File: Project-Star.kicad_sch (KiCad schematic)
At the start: 215 parts, among them J1 J_TH1, J11 J_Flashing, J2 J_TH2, J3 Screw_Terminal_01x01, J4 Screw_Terminal_01x01, J5 Sense Terminals, J6 BMS_I2C, J7 Screw_Terminal_01x01, J8 Screw_Terminal_01x01, Q1 DMN2004K, Q10 ZXMP10A13F, Q13 ZXMP10A13F, Q14 CSD19531Q5A, Q15 CSD19531Q5A, Q16 CSD19531Q5A, Q17 CSD23381F4, Q18 TP0610K-T1-GE3, Q19 BSS138, Q2 DMN2004K, Q20 BSS123, Q3 DMN2004K, Q4 DMN2004K, Q5 CSD19531Q5A, Q6 DMN2004K, Q7 DMN2004K, Q8 DMN2004K, Q9 DMN2004K, SW1 Push_Button, SW2 Push_Button, SW3 SW_DPST, SW4 SW_DPST, U1 BQ7693006DBTR, U11 TPS3839G33DBZR, U2 BQ76200PW, U5 LMT01LPG, U6 MSP430G2553IPW28

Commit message: Restructured Layout
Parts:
- removed C1, C10, C11, C19, C2, C20, C21, C3, C31, C33, C34, C36, C37, C4, C5, C6, C74, C76, C8, C9: 100n, symbol Device:C
- removed C12, C40, C41: 10u, symbol Device:C
- removed C13, C18, C24, C38, C39, C7: 1u, symbol Device:C
- removed C14, C73: 4u7, symbol Device:C
- removed C15, C17: 4n7, symbol Device:C
- removed C16: 370p, symbol Device:C
- removed C22, C23: 10n, symbol Device:C
- removed C32: 2u2, symbol Device:C
- removed C75: 2.2n, symbol Device:C
- removed D1, D13, D18, D19, D20, D4, D61, D62, D63, D64, D7, D9: 5V6, symbol Device:D_Zener_Filled
- removed D10, D12, D14, D15, D29, D3, D31, D5, D6, D65, D66, D67, D68, D69, D70, D71, D8: LED, PCM_Diode_SMD_AKL:D_0805_2012Metric, symbol PCM_SL_Devices:LED
- removed D11, D17, D2, D27, D30: 3V3, symbol Device:D_Zener_Filled
- removed D16, D25, D26, D28, D35: 1N4148W, PCM_Diode_SMD_AKL:D_SOD-123, symbol PCM_Diode_AKL:1N4148W
- removed D24: 18V, symbol Device:D_Zener_Filled
- removed D59, D60: PTVS40VS1UTR, PCM_Diode_SMD_AKL:D_SOD-123F, symbol PCM_Diode_TVS_AKL:PTVS40VS1UTR
- removed E1: SparkGap, symbol Device:SparkGap
- removed FB1, FB2, FB3, FB4: 600R, symbol Device:FerriteBead_Small
- removed J1: J_TH1, 4ms_Connector:Pins_1x02_2.54mm_TH, symbol PCM_4ms_Connector:Conn_01x02
- removed J11: J_Flashing, 4ms_Connector:Pins_2x04_2.54mm_TH, symbol PCM_4ms_Connector:Conn_02x04
- removed J2: J_TH2, 4ms_Connector:Pins_1x02_2.54mm_TH, symbol PCM_4ms_Connector:Conn_01x02
- removed J3, J4, J7, J8: Screw_Terminal_01x01, symbol Connector:Screw_Terminal_01x01
- removed J5: Sense Terminals, 4ms_Connector:Pins_1x09_2.54mm_TH, symbol PCM_4ms_Connector:Conn_01x09
- removed J6: BMS_I2C, symbol Connector_Generic:Conn_01x05
- removed NT1: NetTie_2, symbol Device:NetTie_2
- removed Q1, Q2, Q3, Q4, Q6, Q7, Q8, Q9: DMN2004K, PCM_Package_TO_SOT_SMD_AKL:SOT-23, symbol PCM_Transistor_MOSFET_AKL:DMN2004K
- removed Q10, Q13: ZXMP10A13F, PCM_Package_TO_SOT_SMD_AKL:SOT-23, symbol PCM_Transistor_MOSFET_AKL:ZXMP10A13F
- removed Q14, Q15, Q16, Q5: CSD19531Q5A, Package_TO_SOT_SMD:TDSON-8-1, symbol Transistor_FET:CSD19531Q5A
- removed Q17: CSD23381F4, symbol Device:Q_PMOS
- removed Q18: TP0610K-T1-GE3, PCM_Package_TO_SOT_SMD_AKL:SOT-23, symbol PCM_Transistor_MOSFET_AKL:TP0610K
- removed Q19: BSS138, PCM_Package_TO_SOT_SMD_AKL:SOT-23, symbol PCM_Transistor_MOSFET_AKL:BSS138
- removed Q20: BSS123, PCM_Package_TO_SOT_SMD_AKL:SOT-23, symbol PCM_Transistor_MOSFET_AKL:BSS123
- removed R1, R11, R15, R24, R38, R40, R42, R5, R62, R83, R87: 10k, symbol Device:R
- removed R10, R12, R14, R16, R18, R19, R2, R21, R22, R23, R25, R27, R29, R31, R32, R37, R39, R4, R41, R44, R45, R46, R51, R6, R65, R7, R85, R86, R93, R98: 1k, symbol Device:R
- removed R100, R36, R43, R47, R48, R73, R74, R75, R76, R77, R78, R79, R80, R97, R99: 100R, symbol Device:R
- removed R13, R17, R26, R28, R3, R30, R8, R9: 33R, symbol Device:R
- removed R20: 510k, symbol Device:R
- removed R33, R34: 4k7, symbol Device:R
- removed R49, R50: 4R7, symbol Device:R
- removed R59, R70: 1M, symbol Device:R
- removed R60: 10M, symbol Device:R
- removed R61: 360k, symbol Device:R
- removed R63: 100, symbol Device:R
- removed R64: 3k01, symbol Device:R
- removed R66, R67, R68, R94: 2m, symbol Device:R
- removed R69, R71, R72, R88, R89, R90, R91, R92, R96: 100k, symbol Device:R
- removed R82: 47k, symbol Device:R
- removed R84: 154k, symbol Device:R
- removed R95: 0R, symbol Device:R
- removed SW1, SW2: Push_Button, Button_Switch_THT:SW_PUSH_6mm, symbol PCM_SL_Devices:Push_Button
- removed SW3, SW4: SW_DPST, symbol Switch:SW_DPST
- removed TH1, TH2: 10k NTC, symbol Device:Thermistor
- removed U1: BQ7693006DBTR, Package_SO:TSSOP-30_4.4x7.8mm_P0.5mm, symbol Battery_Management:BQ76930DBT
- removed U11: TPS3839G33DBZR, Package_TO_SOT_SMD:SOT-23, symbol Power_Supervisor:TPS3839DBZ
- removed U2: BQ76200PW, Package_SO:TSSOP-16_4.4x5mm_P0.65mm, symbol Battery_Management:BQ76200PW
- removed U5: LMT01LPG, Package_TO_SOT_THT:TO-92-2, symbol Sensor_Temperature:LMT01LPG
- removed U6: MSP430G2553IPW28, Package_SO:TSSOP-28_4.4x9.7mm_P0.65mm, symbol MCU_Texas_MSP430:MSP430G2553IPW28
- added J12, J13: Screw_Terminal_01x01, symbol Connector:Screw_Terminal_01x01
- added J9: Sense Terminals, 4ms_Connector:Pins_1x09_2.54mm_TH, symbol PCM_4ms_Connector:Conn_01x09
- added SW5: SW_DPST, symbol Switch:SW_DPST
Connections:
- net C0: now also J9.1 (Pin_1)
- net C1: now also J9.2 (Pin_2)
- net C2: now also J9.3 (Pin_3)
- net C3: now also J9.4 (Pin_4)
- net C4: now also J9.5 (Pin_5)
- net C5: now also J9.6 (Pin_6)
- net C6: now also J9.7 (Pin_7)
- net C7: now also J9.8 (Pin_8)
- net C8: now also J9.9 (Pin_9)
- net SCREW_BATT+: now also SW5.4
- new net: J13.1 (Pin_1), SW5.1
- new net: J12.1 (Pin_1), SW5.3
- new net SCREW_BATT-: SW5.2
- no-connect marks 1 -> 0
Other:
- added sheet BMS Protection Board (BMS Protection Board.kicad_sch)
- sheet USB-C-PD3.0 ports: added none; removed I2Ct_SCL, I2Ct_SDA
- note removed: "BMS Protection Board for 8S Battery Pack In/Out: min voltage: 24.0 V, nominal voltage: 29.6 V, max voltage: 33.6 V Output: 30A continuous discharge current, 100A peak discharge current"
- note removed: "Balancing & BMC"
- note removed: "Battery Level LEDs"
- note removed: "Battery Management System Controller"
- note removed: "CONN Headers"
- note removed: "Current Sense Filtering"
- note removed: "From TIDA-00449"
- note removed: "From TIDA-00449 / TIDA-010030"
- note removed: "From slua749a"
- note removed: "From slua810"
- note removed: "From slusc16b"
- note removed: "From slva729a"
- note removed: "From slva729a VDDCP was picked"
- note removed: "High Voltage REGSRC Supply"
- note removed: "High-Side Gate Driver"
- note removed: "I2C Pullups"
- note removed: "Interrupt for new current readings or errors"
- note removed: "JTAG/SBW"
- note removed: "MCU Current Sense"
- note removed: "PD I2C Lines have pullup's already"
- note removed: "PWR FLAGs"
- note removed: "Pack Switching and Current Sensing"
- note removed: "Passive Balancing Circuit"
- note removed: "REGOUT supplys 3v3"
- note removed: "Read Voltage"
- note removed: "Screw Terminals"
- note removed: "TODO: Add USB-C to Flash board"
- note removed: "Temperature Sensor"
- note removed: "Thermistors"
- note removed: "Understand how this works"
- note removed: "VC0-VSS (Vin max 3V6)"
- note removed: "Voltage Supervisor"
- note removed: "Wake-Up"
- note removed: "from TIDA-010030"
- note removed: "from slua810"
- note removed: "system is on LED"

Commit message: worked on MCU
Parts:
- added J3, J4: Screw_Terminal_01x01, symbol Connector:Screw_Terminal_01x01
- added SW2: SW_DPST, symbol Switch:SW_DPST
- renumbered J12 to J1, J13 to J2, J9 to J5, SW5 to SW1
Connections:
- net PACK+: now also SW2.4
- net PACK-: now also SW2.2
- net SCREW_BATT+ renamed BATT+
- net SCREW_BATT- renamed BATT-
- new net: J4.1 (Pin_1), SW2.1
- new net: J3.1 (Pin_1), SW2.3
- no-connect marks 0 -> 2
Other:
- removed sheet USB-C-PD3.0
- added sheet Power Management System Controller (Power Management System Controller.kicad_sch)
- added sheet USB-C PD 3.0 Source (USB-C PD 3.0 Source.kicad_sch)
- added sheet USB-C PD 3.1 Sink (USB-C PD 3.1 Sink.kicad_sch)
- sheet BMS Protection Board ports: added ALERT, BATT+, BATT-, CHG_EN, CP_EN, DSG_EN, ISENSE, PACK_READ_STATS, PACK_V, PCHG_EN, READ_ISENSE, REGOUT, SCL, SDA, TEMP, WAKE; removed SCREW_BATT+, SCREW_BATT-
- moved on the sheet: J1, J2, J5, SW1

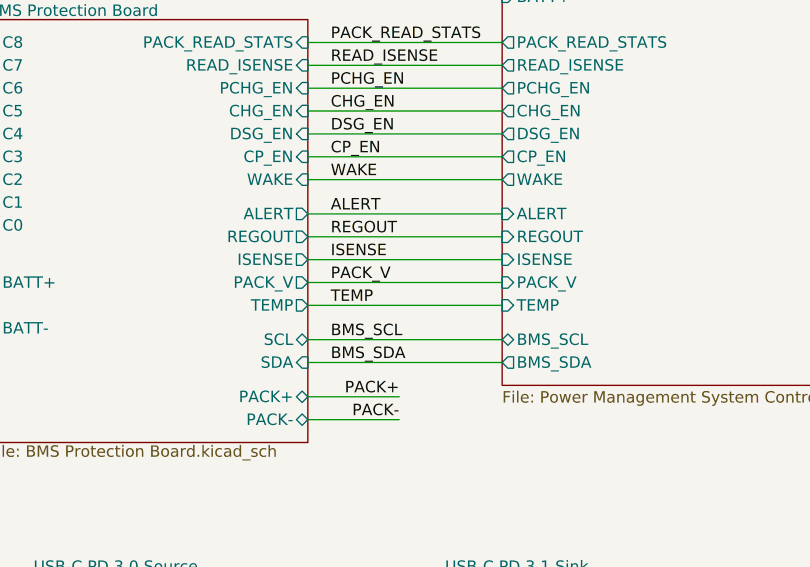
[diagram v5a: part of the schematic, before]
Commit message: commit before simplifying and removing features
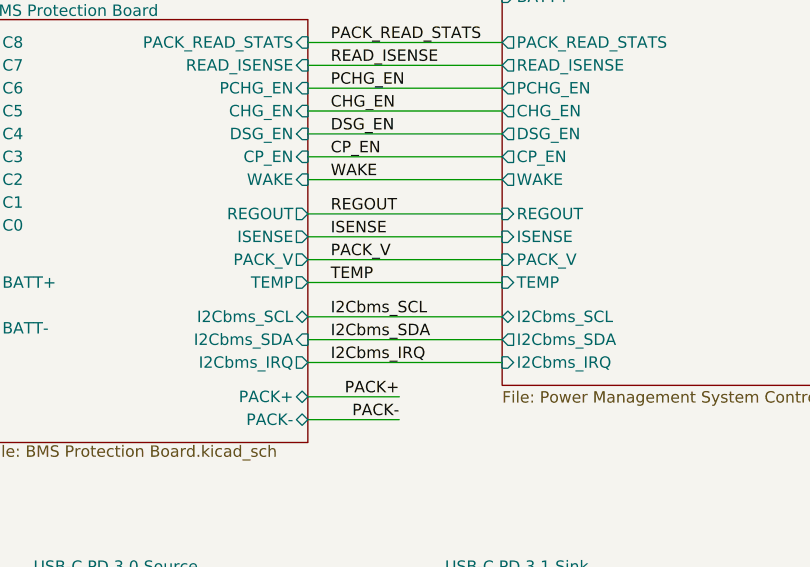
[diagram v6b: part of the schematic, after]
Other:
- sheet BMS Protection Board ports: added I2Cbms_IRQ, I2Cbms_SCL, I2Cbms_SDA; removed ALERT, SCL, SDA
- sheet Power Management System Controller ports: added I2Cbms_IRQ, I2Cbms_SCL, I2Cbms_SDA; removed ALERT, BMS_SCL, BMS_SDA

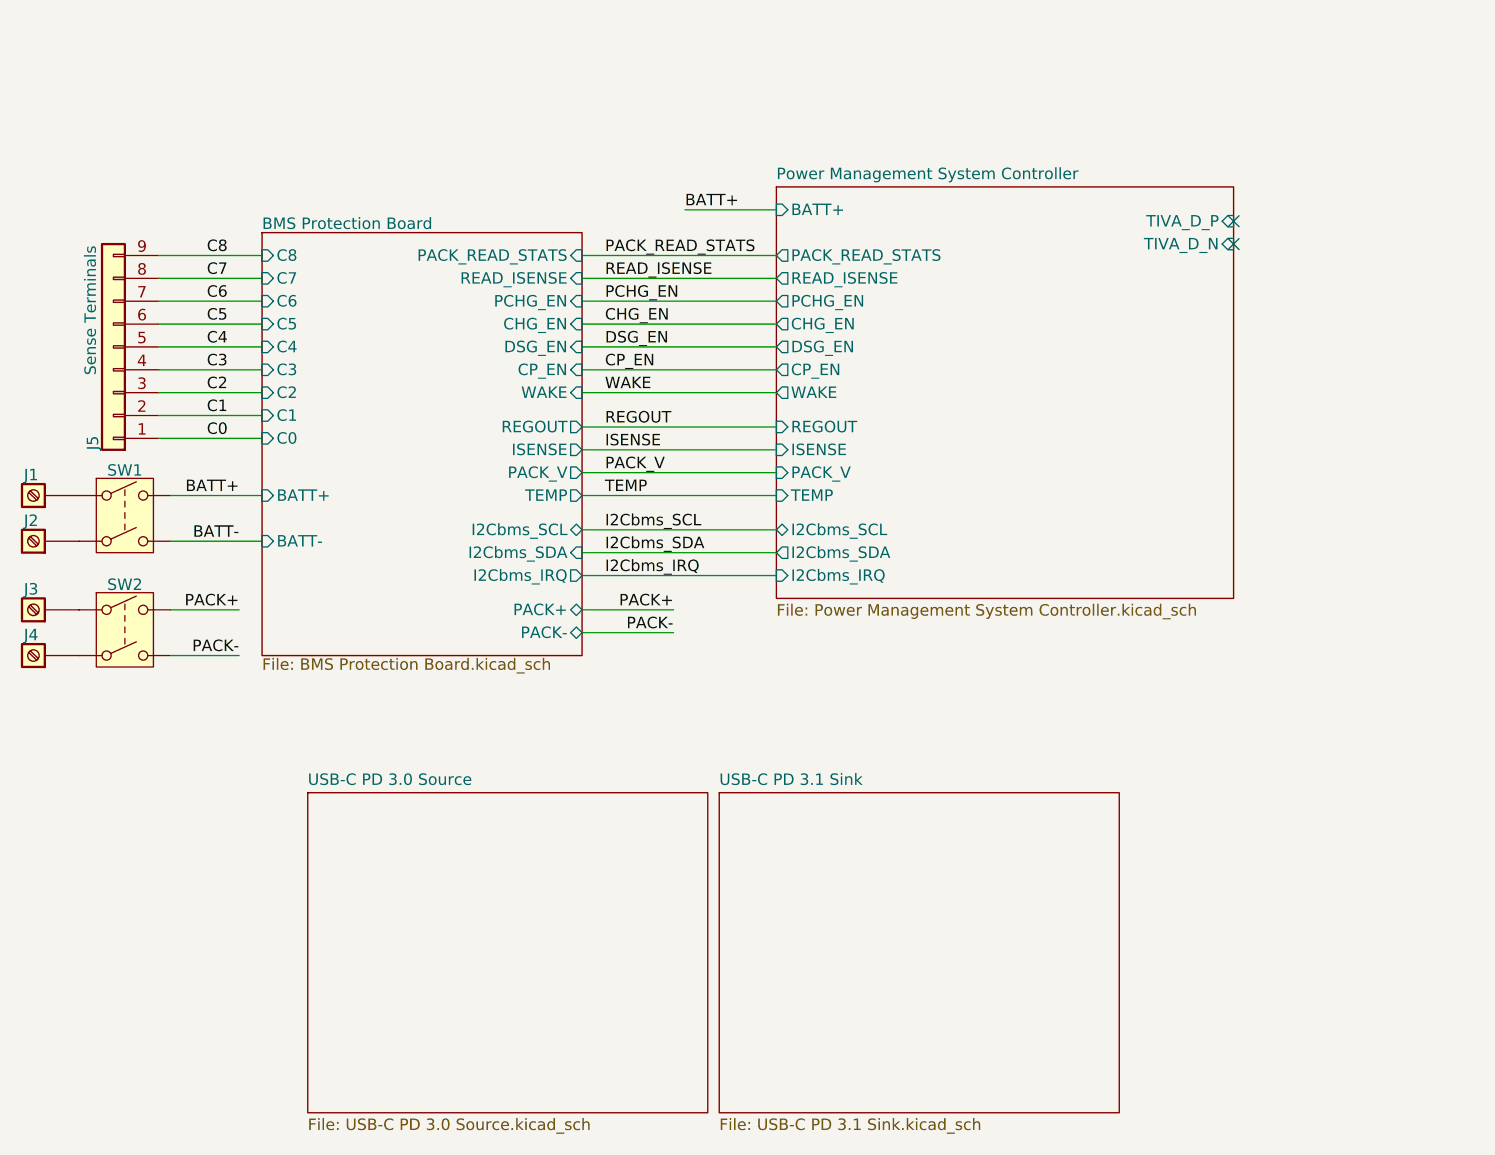
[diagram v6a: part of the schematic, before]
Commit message: Added Fuel/Gas Guage
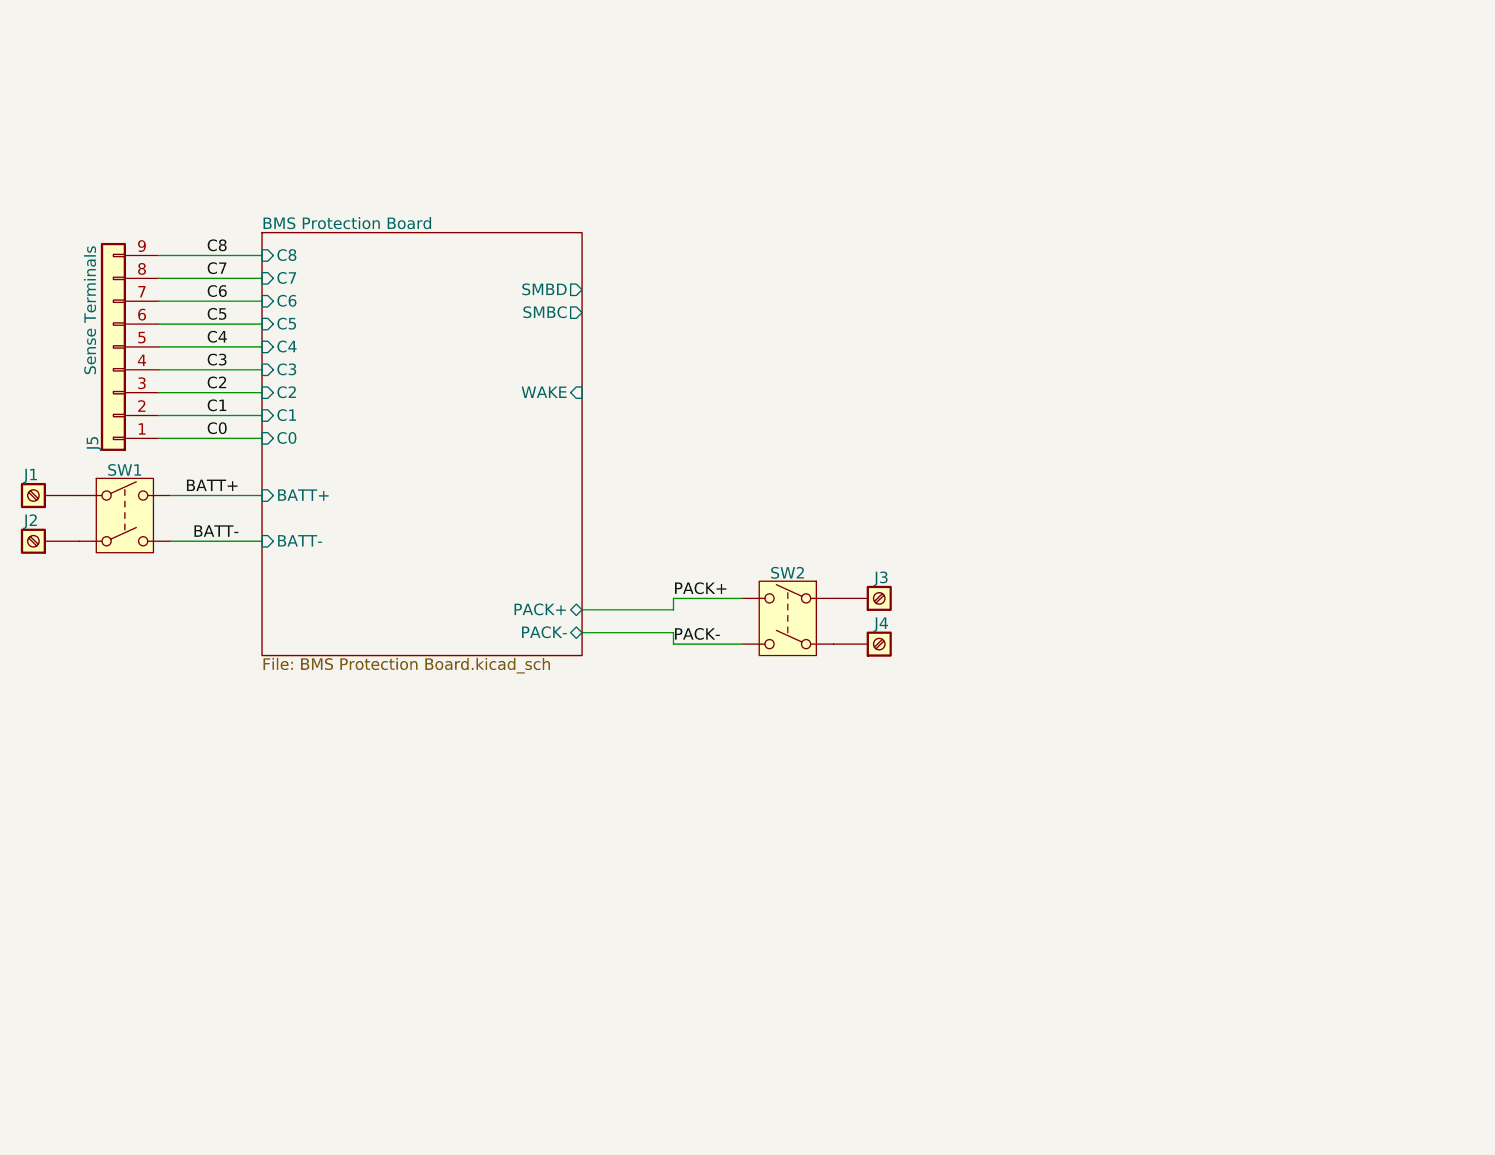
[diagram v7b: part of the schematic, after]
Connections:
- no-connect marks 2 -> 0
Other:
- removed sheet Power Management System Controller
- removed sheet USB-C PD 3.0 Source
- removed sheet USB-C PD 3.1 Sink
- sheet BMS Protection Board ports: added SMBC, SMBD; removed CHG_EN, CP_EN, DSG_EN, I2Cbms_IRQ, I2Cbms_SCL, I2Cbms_SDA, ISENSE, PACK_READ_STATS, PACK_V, PCHG_EN, READ_ISENSE, REGOUT, TEMP
- moved on the sheet: J3, J4, SW2

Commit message: ready to start first pass review on bms
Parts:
- added J4: SMB, symbol Connector_Generic:Conn_01x03
- renumbered J5 to J3, J3 to J5, J4 to J6
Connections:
- net PACK-: now also J4.3 (Pin_3)
- new net SMBC: J4.1 (Pin_1)
- new net SMBD: J4.2 (Pin_2)
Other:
- sheet BMS Protection Board ports: added none; removed WAKE
- moved on the sheet: J5, J6, SW2
